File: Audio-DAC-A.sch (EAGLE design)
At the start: 125 parts, among them IC1 7833, IC10 NJM2114, IC11 7812, IC12 7812, IC13 78L09, IC2 7805, IC3 7805, IC4 7833, IC5 7812, IC6 AK4493EQ, IC7 7812, IC8 7912, IC9 NJM2114, Q5 NPN2SC3422, Q6 PNP2SA1359, Q7 NPN2SC3422, Q8 PNP2SA1359, Q9 NPN2SC3325, SW1 12V, X1 22.5792MHz, X2 24.576MHz

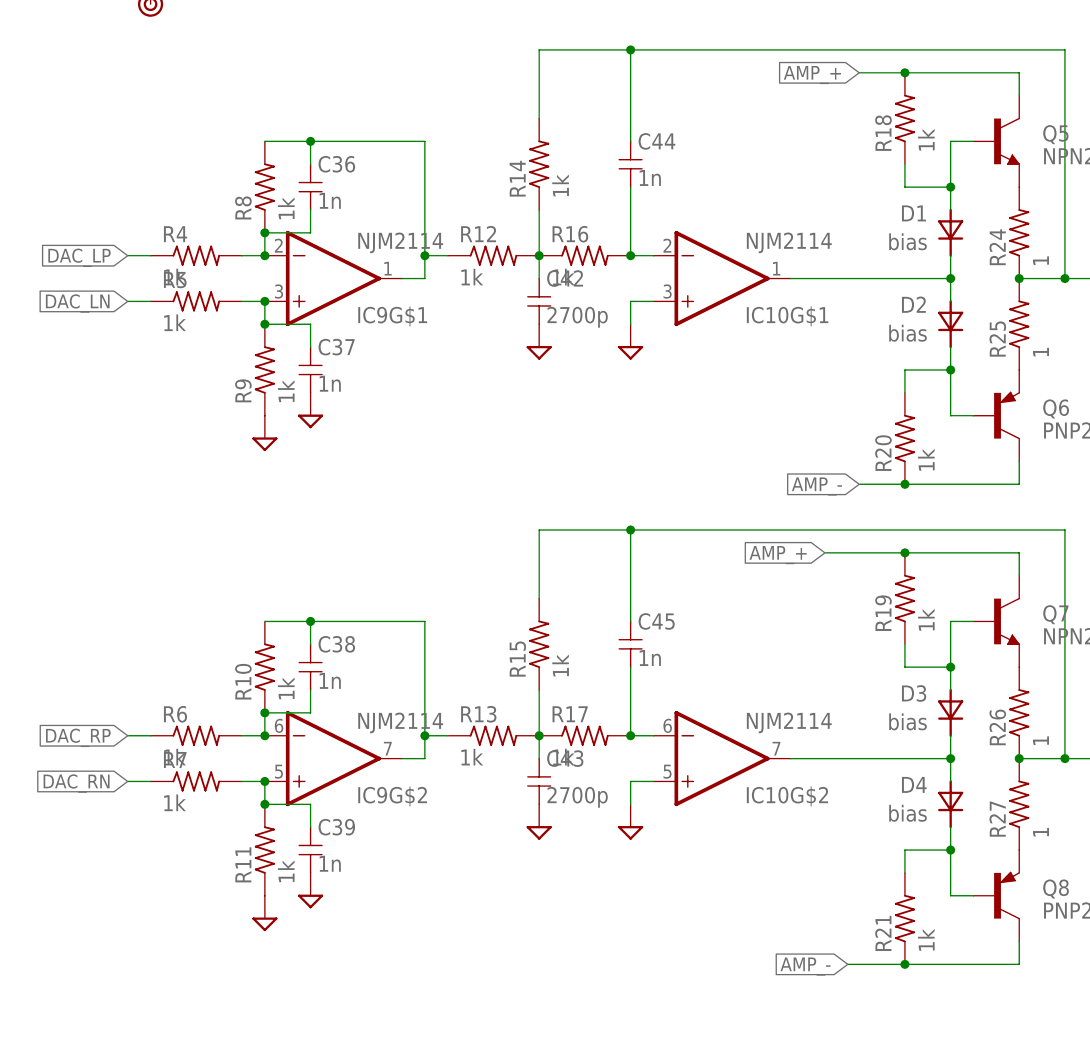
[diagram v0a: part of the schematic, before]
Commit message: 回路図を修正
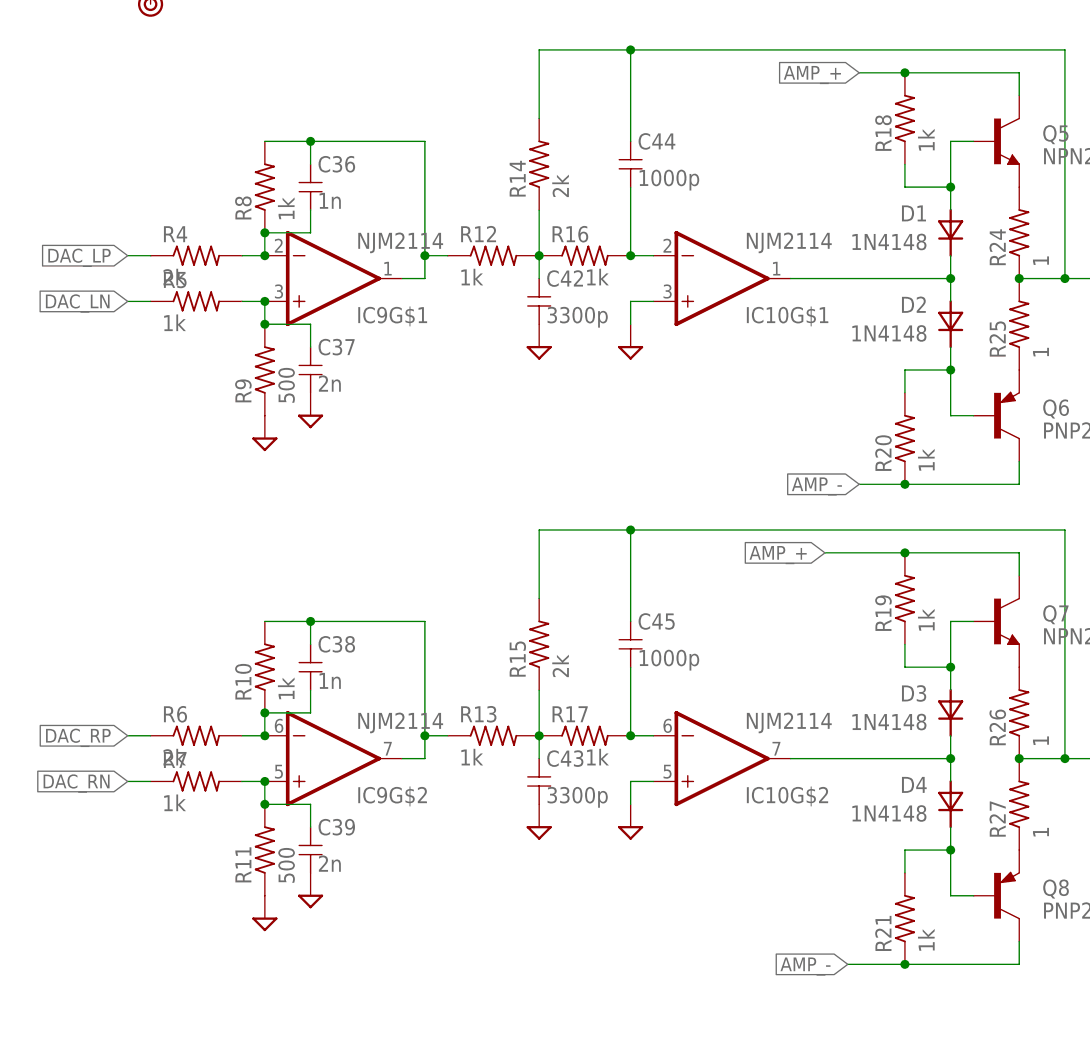
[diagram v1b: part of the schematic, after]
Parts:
- C37, C39: value 1n -> 2n
- C42, C43: value 2700p -> 3300p
- C44, C45: value 1n -> 1000p
- D1, D2, D3, D4: value bias -> 1N4148
- R11, R9: value 1k -> 500
- R14, R15, R4, R6: value 1k -> 2k
